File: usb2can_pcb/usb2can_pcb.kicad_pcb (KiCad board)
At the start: 2 copper layers, 26.1 x 15 mm, 19 parts, among them J1 USB_C_Receptacle_USB2.0, J2 CAN, J3 CAN, U1 XC6206P332MR, U2 STM32F072C8T6, U3 MAX3051

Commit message: add customer number placeholder for JLCPCB
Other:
- board text added: "JLCJLCJLCJLC"
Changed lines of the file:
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@@
     (effects (font (size 1 1) (thickness 0.15)))
+  )
+  (gr_text "JLCJLCJLCJLC" (at 40.8432 60.6552 90) (layer "F.SilkS")
+    (effects (font (size 0.8 0.8) (thickness 0.15)))
   )
   (gr_text "BO" (at 44.0436 54.4576 90) (layer "F.SilkS")

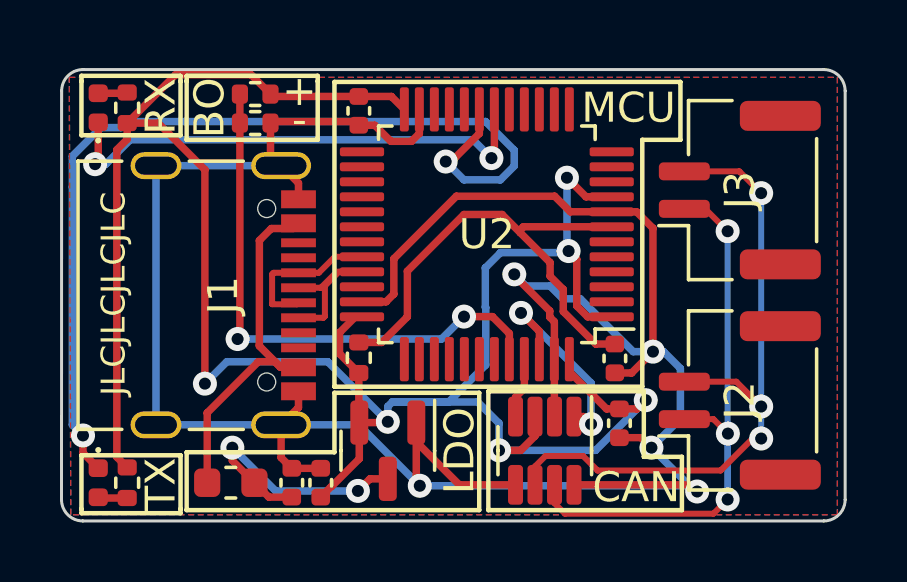
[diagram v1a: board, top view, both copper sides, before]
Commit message: fix CAN connector pin assign problem
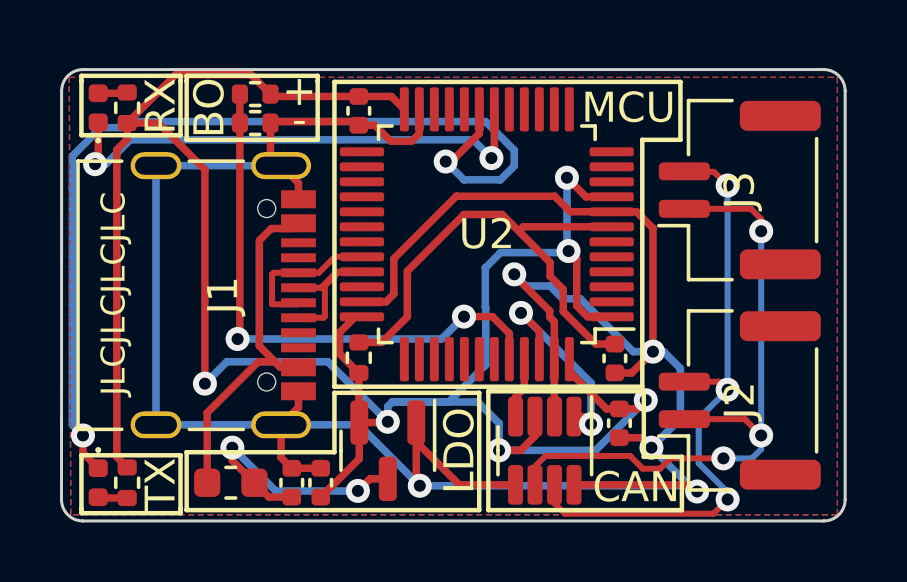
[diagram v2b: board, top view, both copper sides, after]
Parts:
- C2, C3: value 10uF -> 1uF
- R4, R5: value 120R -> 510R
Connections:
- J2 pad 1: /CAN+ -> /CAN-
- J2 pad 2: /CAN- -> /CAN+
- J3 pad 1: /CAN+ -> /CAN-
- J3 pad 2: /CAN- -> /CAN+
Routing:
- net /CAN-: track 22.9 -> 21.9 mm
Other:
- board text added: "V1.1"
- board text removed: "V1.0"
